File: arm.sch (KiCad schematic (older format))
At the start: 96 parts, among them J1 MICROSD_SOCKET_SPI, M1 MOTOR, P1 MicroUSB, P2 HC-05/06, Q1 MOSFET_N, Q2 IRLML2246TRPBF, Q3 IRLML2246TRPBF, Q5 IRLML2246TRPBF, Q6 IRLML2246TRPBF, Q7 IRLML2246TRPBF, Q8 IRLML2246TRPBF, Q9 IRLML2246TRPBF, U3 LTC2942-1, U4 HMC5883L, U5 MPU6050, U7 BMP085, X1 8 mHz, X2 32.768(MS3V-T1R)

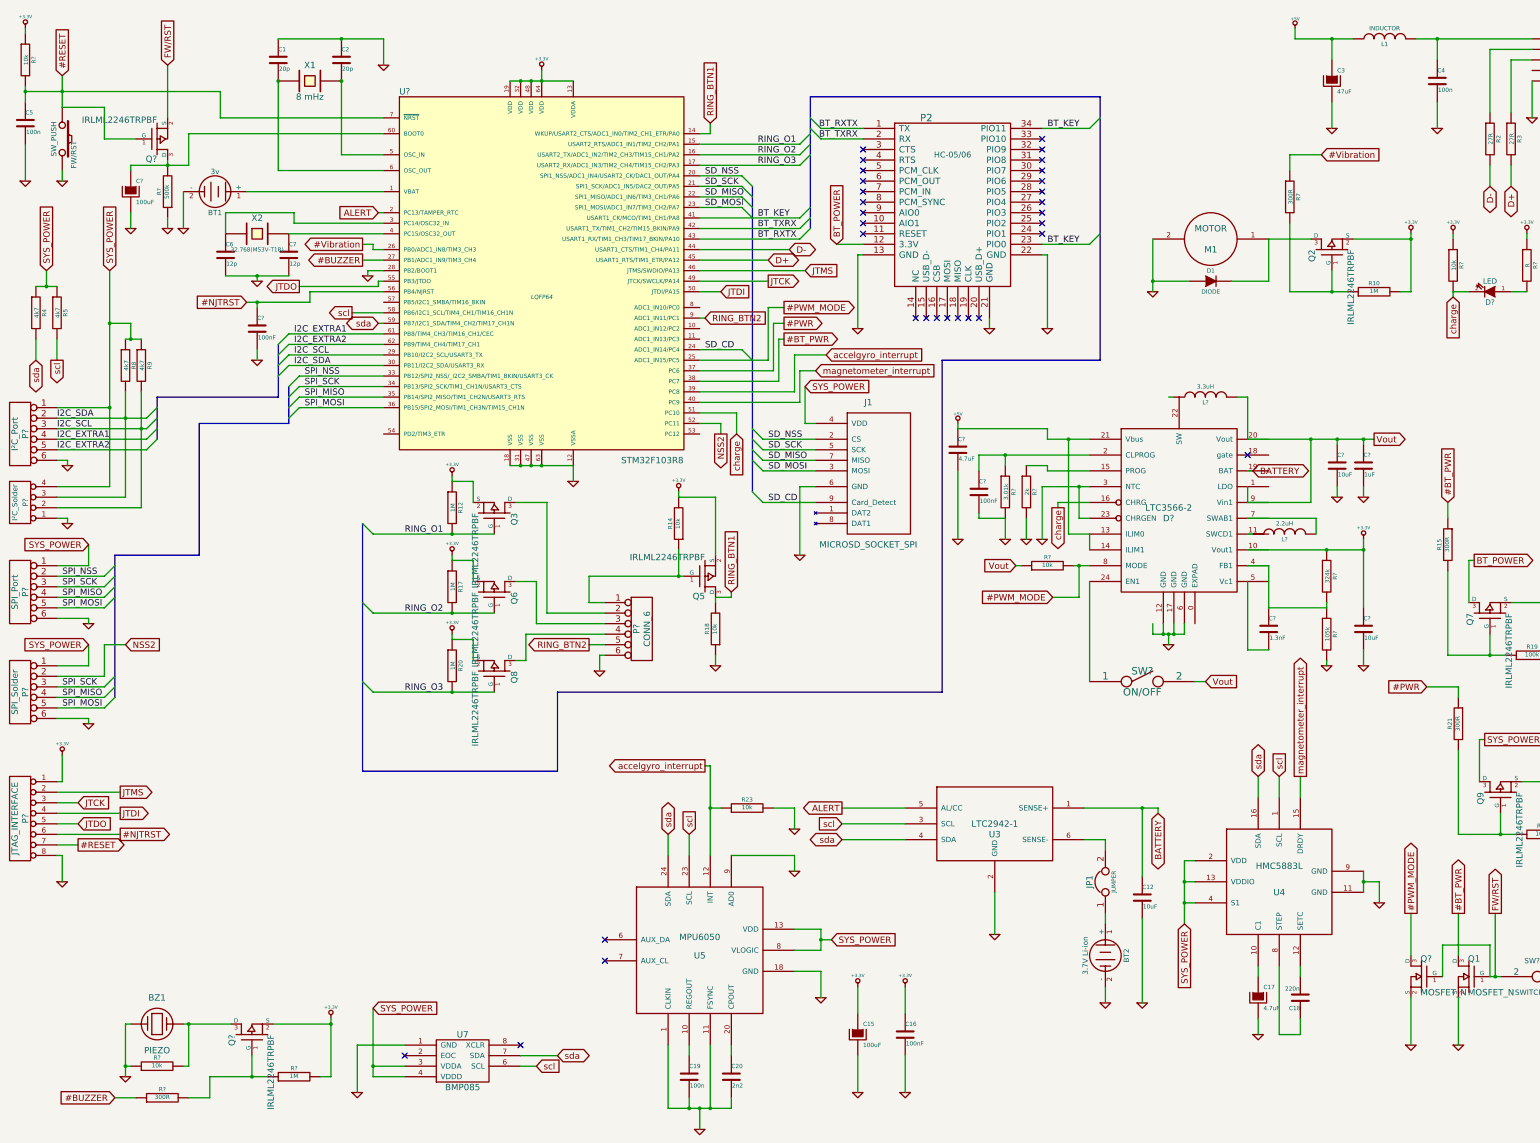
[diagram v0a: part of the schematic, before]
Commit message: new look for inverted global labels (using "~" instead of "#")
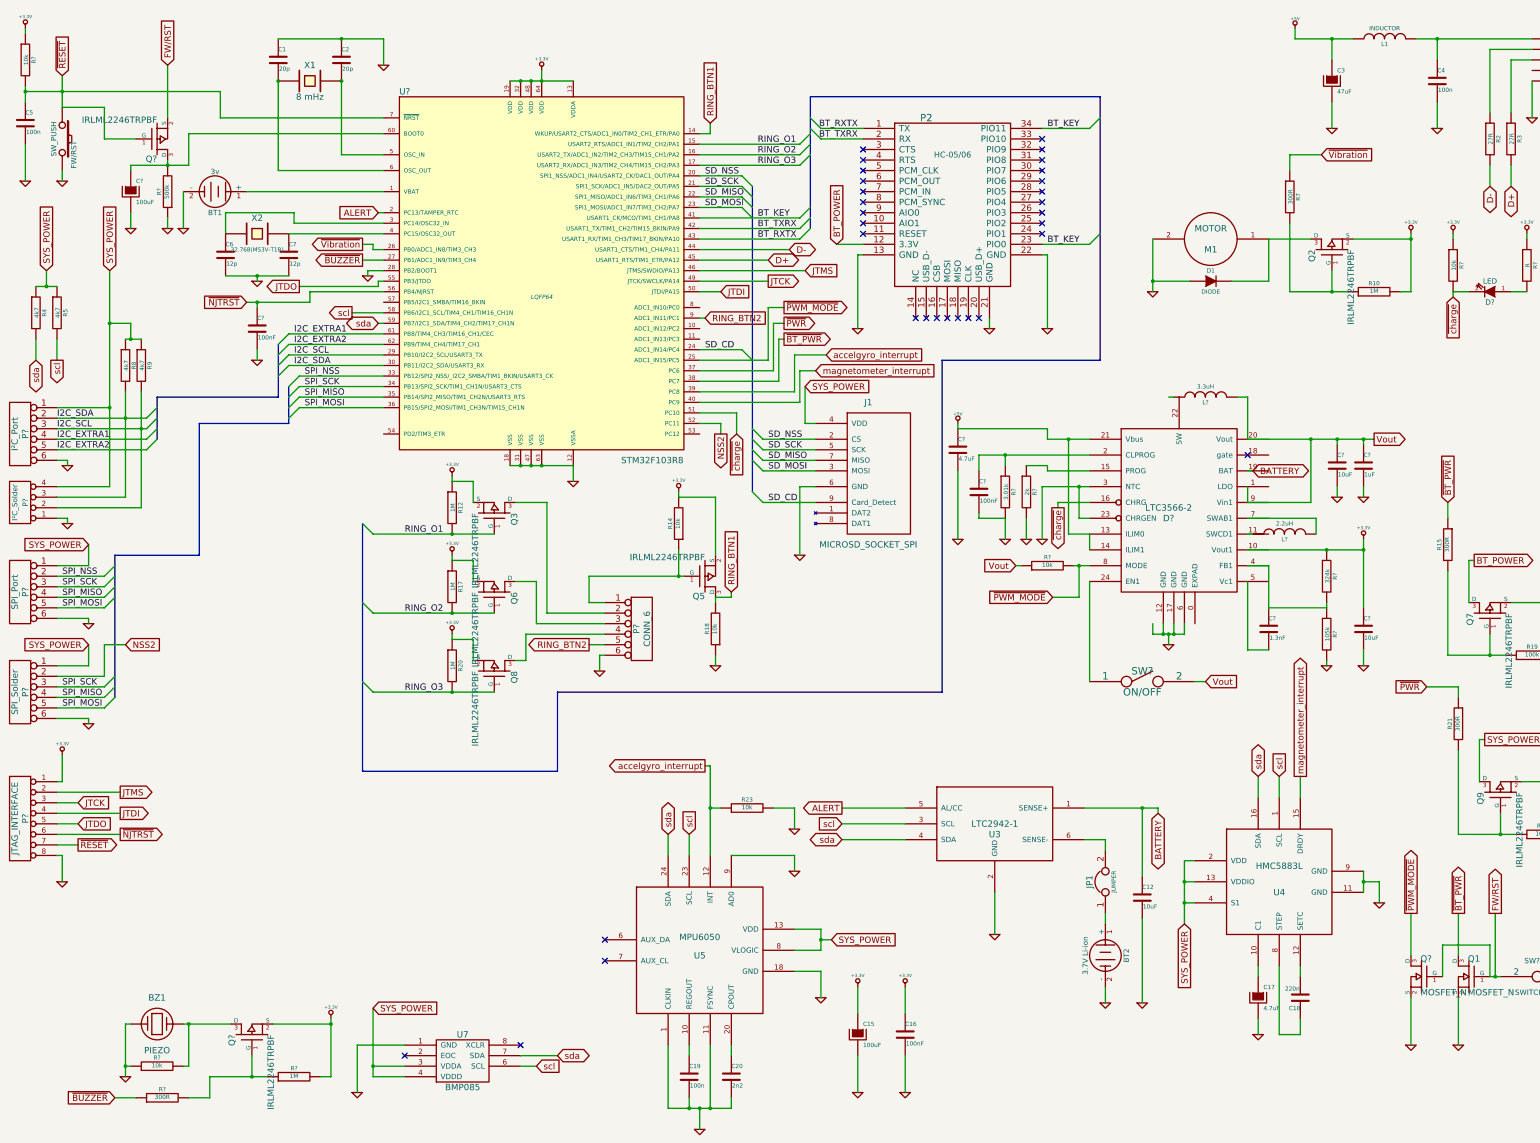
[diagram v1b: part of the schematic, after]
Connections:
- net #BT_PWR renamed ~BT_PWR
- net #BUZZER renamed ~BUZZER
- net #NJTRST renamed ~NJTRST
- net #PWM_MODE renamed ~PWM_MODE
- net #PWR renamed ~PWR
- net #RESET renamed ~RESET
- net #Vibration renamed ~Vibration
- net charge renamed ~charge
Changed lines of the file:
@@
 $EndComp
 Text GLabel 10500 5200 3    60   Output ~ 0
-charge
+~charge
 $Comp
 L C C5
@@
 $EndComp
 Text GLabel 7900 3600 2    60   Output ~ 0
-#BT_PWR
+~BT_PWR
 Text GLabel 4050 2400 0    60   Input ~ 0
 ALERT
@@
 $EndComp
 Text GLabel 3900 2700 0    60   Output ~ 0
-#Vibration
+~Vibration
 $Comp
 L +3.3V #PWR033
@@
 $EndComp
 Text GLabel 13000 1850 2    60   Input ~ 0
-#Vibration
+~Vibration
 $Comp
 L MOSFET_P Q3
@@
 $EndComp
 Text GLabel 14200 5150 1    60   Input ~ 0
-#BT_PWR
+~BT_PWR
 $Comp
 L R R15
@@
 $EndComp
 Text GLabel 7900 3450 2    60   Output ~ 0
-#PWR
+~PWR
 $Comp
 L +3.3V #PWR038
@@
 SYS_POWER
 Text GLabel 14000 6900 0    60   Input ~ 0
-#PWR
+~PWR
 $Comp
 L CAPAPOL C11
@@
 SD_CD
 Text GLabel 14300 9050 1    60   Output ~ 0
-#BT_PWR
+~BT_PWR
 Entry Wire Line
 	8050 2550 8150 2450
@@
 $EndComp
 Text GLabel 14250 3200 3    60   Input ~ 0
-charge
+~charge
 $Comp
 L LED D?
@@
 $EndComp
 Text GLabel 1550 10800 0    60   Input ~ 0
-#BUZZER
+~BUZZER
 $Comp
 L MOSFET_P Q?
@@
 $EndComp
 Text GLabel 3900 2850 0    60   Output ~ 0
-#BUZZER
+~BUZZER
 $Comp
 L +3.3V #PWR062
@@
 $EndComp
 Text GLabel 10450 6050 0    60   Input ~ 0
-#PWM_MODE
+~PWM_MODE
 Text GLabel 13850 9050 1    60   Output ~ 0
-#PWM_MODE
+~PWM_MODE
 $Comp
 L MOSFET_N Q?
@@
 NSS2
 Text GLabel 7900 3300 2    60   Output ~ 0
-#PWM_MODE
+~PWM_MODE
 $Comp
 L CONN_6 P?
@@
 JTDO
 Text GLabel 2800 3250 0    60   Input ~ 0
-#NJTRST
+~NJTRST
 $Comp
 L C C?
@@
 $EndComp
 Text GLabel 1050 1100 1    60   Input ~ 0
-#RESET
+~RESET
 $Comp
 L CONN_8 P?
@@
 $EndComp
 Text GLabel 1200 8400 2    60   Output ~ 0
-#RESET
+~RESET
 Text GLabel 1600 8300 2    60   Output ~ 0
-#NJTRST
+~NJTRST
 Text GLabel 1200 8200 2    60   Input ~ 0
 JTDO
@@
 BT_KEY
 Text GLabel 7450 4500 3    60   Input ~ 0
-charge
+~charge
 Text GLabel 6050 6500 0    60   Output ~ 0
 RING_BTN2

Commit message: new names for global labels because Alex-Daniel wanted so -_-
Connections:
- net accelgyro_interrupt renamed MPU_INT
- net magnetometer_interrupt renamed HMC_INT
- net scl renamed SCL
- net sda renamed SDA
- net ~BT_PWR renamed ~BT_PWR_ENABLE
- net ~PWR renamed ~SYS_PWR_ENABLE
- net ~Vibration renamed ~VIBRATION
- net ~charge renamed ~CHARGE
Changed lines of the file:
@@
 L GND #PWR02
 U 1 1 52C0BA78
-P 8600 3500
-F 0 "#PWR02" H 8600 3500 30  0001 C CNN
-F 1 "GND" H 8600 3430 30  0001 C CNN
-F 2 "" H 8600 3500 60  0000 C CNN
-F 3 "" H 8600 3500 60  0000 C CNN
-	1    8600 3500
+P 8600 3150
+F 0 "#PWR02" H 8600 3150 30  0001 C CNN
+F 1 "GND" H 8600 3080 30  0001 C CNN
+F 2 "" H 8600 3150 60  0000 C CNN
+F 3 "" H 8600 3150 60  0000 C CNN
+	1    8600 3150
 	1    0    0    -1
 $EndComp
@@
 $EndComp
 Text GLabel 4050 3450 0    60   BiDi ~ 0
-sda
+SDA
 Text GLabel 3800 3350 0    60   Output ~ 0
-scl
+SCL
 $Comp
 L R R4
@@
 $EndComp
 Text GLabel 12400 7750 1    60   BiDi ~ 0
-sda
+SDA
 Text GLabel 12600 7750 1    60   Input ~ 0
-scl
+SCL
 Text GLabel 6800 8300 1    60   BiDi ~ 0
-sda
+SDA
 Text GLabel 7000 8300 1    60   Input ~ 0
-scl
-Text GLabel 5750 10400 2    60   BiDi ~ 0
-sda
+SCL
+Text GLabel 5900 10400 2    60   BiDi ~ 0
+SDA
 Text GLabel 5550 10500 2    60   Input ~ 0
-scl
+SCL
 $Comp
 L CAPAPOL C17
@@
 $EndComp
 Text GLabel 7150 7650 0    60   Output ~ 0
-accelgyro_interrupt
+MPU_INT
 $Comp
 L R R23
@@
 $EndComp
 Text GLabel 8300 3750 2    60   Input ~ 0
-accelgyro_interrupt
+MPU_INT
 $Comp
 L GND #PWR018
@@
 $EndComp
 Text GLabel 10500 5200 3    60   Output ~ 0
-~charge
+~CHARGE
 $Comp
 L C C5
@@
 $EndComp
 Text GLabel 7900 3600 2    60   Output ~ 0
-~BT_PWR
+~BT_PWR_ENABLE
 Text GLabel 4050 2400 0    60   Input ~ 0
 ALERT
@@
 $EndComp
 Text GLabel 8450 8350 0    60   BiDi ~ 0
-sda
+SDA
 Text GLabel 8450 8200 0    60   Input ~ 0
-scl
+SCL
 Text GLabel 8450 8050 0    60   Output ~ 0
 ALERT
@@
 $EndComp
 Text GLabel 3900 2700 0    60   Output ~ 0
-~Vibration
+~VIBRATION
 $Comp
 L +3.3V #PWR033
@@
 $EndComp
 Text GLabel 13000 1850 2    60   Input ~ 0
-~Vibration
+~VIBRATION
 $Comp
 L MOSFET_P Q3
@@
 $EndComp
 Text GLabel 14200 5150 1    60   Input ~ 0
-~BT_PWR
+~BT_PWR_ENABLE
 $Comp
 L R R15
@@
 $EndComp
 Text GLabel 7900 3450 2    60   Output ~ 0
-~PWR
+~SYS_PWR_ENABLE
 $Comp
 L +3.3V #PWR038
@@
 SYS_POWER
 Text GLabel 14000 6900 0    60   Input ~ 0
-~PWR
+~SYS_PWR_ENABLE
 $Comp
 L CAPAPOL C11
@@
 Text GLabel 4000 9950 2    60   Input ~ 0
 SYS_POWER
-Text GLabel 11700 9150 3    60   Input ~ 0
+Text GLabel 11700 8350 1    60   Input ~ 0
 SYS_POWER
 Text GLabel 8100 4050 2    60   Input ~ 0
@@
 Text Label 7750 5150 0    60   ~ 0
 SD_CD
-Text GLabel 14300 9050 1    60   Output ~ 0
-~BT_PWR
+Text GLabel 14300 9150 1    60   Output ~ 0
+~BT_PWR_ENABLE
 Entry Wire Line
 	8050 2550 8150 2450
@@
 $EndComp
 Text GLabel 800  3800 3    60   BiDi ~ 0
-sda
+SDA
 Text GLabel 1000 3800 3    60   Output ~ 0
-scl
+SCL
 $Comp
 L R R17
@@
 $EndComp
 Text GLabel 12800 7750 1    60   Output ~ 0
-magnetometer_interrupt
+HMC_INT
 Text GLabel 8200 3900 2    60   Input ~ 0
-magnetometer_interrupt
+HMC_INT
 $Comp
 L MOSFET_N Q1
@@
 $EndComp
 Text GLabel 14250 3200 3    60   Input ~ 0
-~charge
+~CHARGE
 $Comp
 L LED D?
@@
 	1    0    0    -1
 $EndComp
-Text GLabel 14650 9050 1    60   Output ~ 0
+Text GLabel 14650 9150 1    60   Output ~ 0
 FW/RST
 $Comp
@@
 Text GLabel 10450 6050 0    60   Input ~ 0
 ~PWM_MODE
-Text GLabel 13850 9050 1    60   Output ~ 0
+Text GLabel 13850 9150 1    60   Output ~ 0
 ~PWM_MODE
 $Comp
@@
 BT_KEY
 Text GLabel 7450 4500 3    60   Input ~ 0
-~charge
+~CHARGE
 Text GLabel 6050 6500 0    60   Output ~ 0
 RING_BTN2
@@
 	14300 9850 14300 10300
 Wire Wire Line
-	14300 9050 14300 9450
-Wire Wire Line
 	8100 4400 8100 4050
 Wire Wire Line
@@
 	11700 8950 11800 8950
 Wire Wire Line
-	11700 8550 11700 9150
+	11700 8950 11700 8350
 Wire Wire Line
 	11800 8550 11700 8550
@@
 	4000 10600 4300 10600
 Wire Wire Line
-	5400 10400 5750 10400
+	5400 10400 5900 10400
 Wire Wire Line
 	9900 8850 9900 9250
 Wire Wire Line
-	8600 2800 8600 3500
-Wire Wire Line
 	8650 2800 8600 2800
 Wire Wire Line
@@
 	15700 9000 15700 9550
 Wire Wire Line
-	14650 9650 14650 9050
-Wire Wire Line
 	2250 1650 4100 1650
 Wire Wire Line
@@
 	13850 9850 13850 10300
 Wire Wire Line
-	13850 9050 13850 9450
-Wire Wire Line
 	14600 9650 14600 9350
 Wire Wire Line
@@
 Wire Wire Line
 	11800 8750 11700 8750
-Connection ~ 11700 8950
 Wire Wire Line
 	1050 7550 1050 7800
@@
 Wire Wire Line
 	7450 4300 7450 4500
+Connection ~ 11700 8550
+Wire Wire Line
+	14650 9150 14650 9650
+Wire Wire Line
+	14300 9150 14300 9450
+Wire Wire Line
+	13850 9150 13850 9450
+Wire Wire Line
+	8600 2800 8600 3150
 $EndSCHEMATC
